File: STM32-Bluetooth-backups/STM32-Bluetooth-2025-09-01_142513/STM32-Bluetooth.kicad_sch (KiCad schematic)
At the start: 41 parts, among them J1 USB_C_Receptacle_USB2.0_16P, J2 TC2030, J3 Conn_01x04, J4 Conn_Coaxial, SW1 SW_Push, U2 STM32WB55CEU6, U3 MIC5365-3.3YD5, X1 32MHz, X2 32kHz768

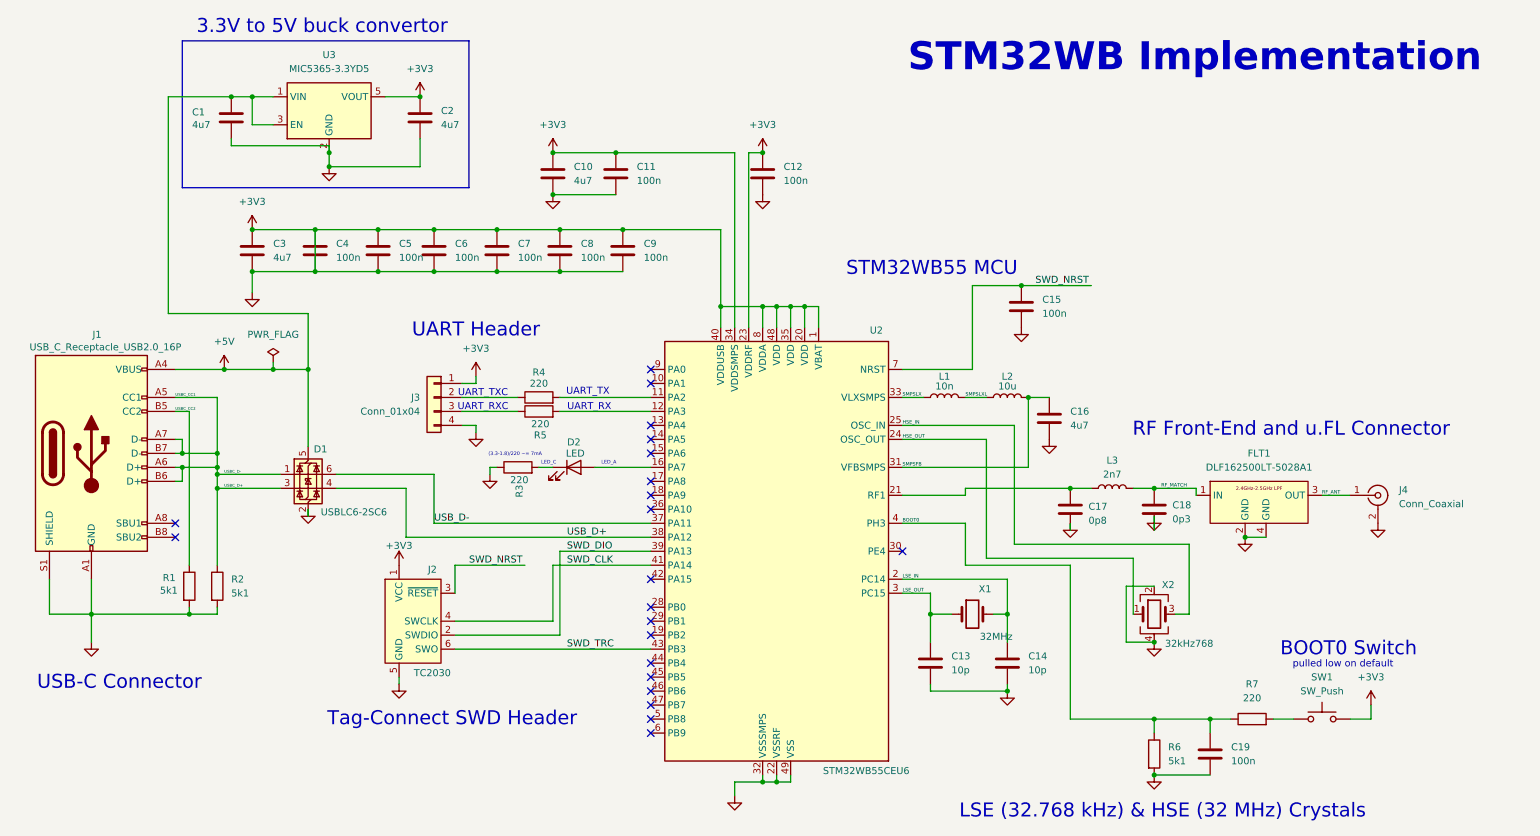
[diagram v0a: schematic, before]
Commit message: Adding net classes and editing footprint library
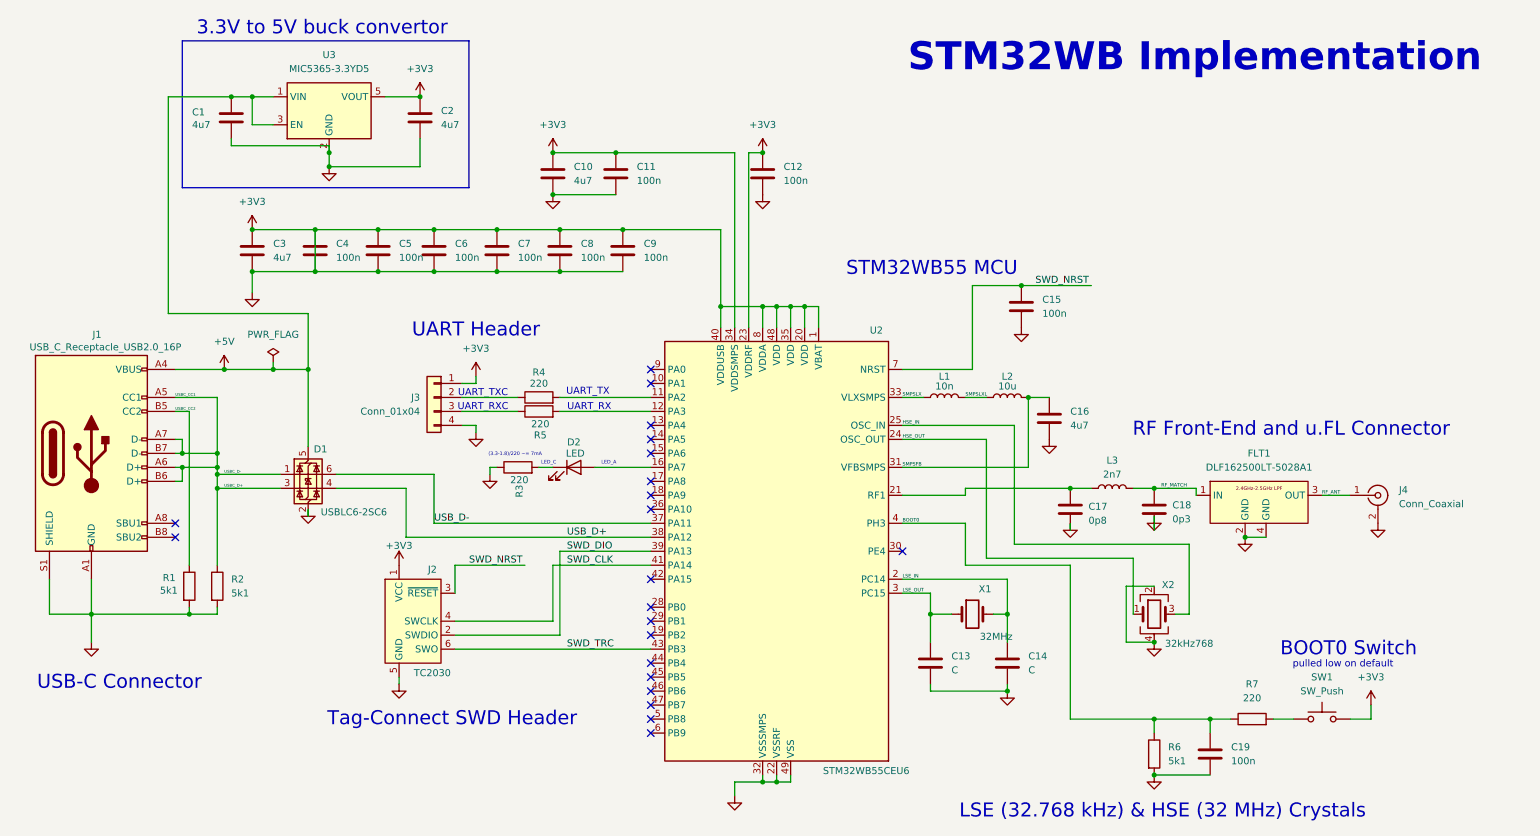
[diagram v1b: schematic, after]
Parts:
- C1, C10, C16, C2, C3: footprint Capacitor_SMD:C_0603_1608Metric -> (none)
- C11, C12, C15, C17, C18, C19, C4, C5, C6, C7, C8, C9: footprint Capacitor_SMD:C_0402_1005Metric -> (none)
- C13, C14: value 10p -> C; footprint Capacitor_SMD:C_0402_1005Metric -> (none)
- D2: footprint LED_SMD:LED_0402_1005Metric -> (none)
- J1: footprint Connector_USB:USB_C_Receptacle_GCT_USB4105-xx-A_16P_TopMnt_Horizontal -> (none)
- J3: footprint Connector_Molex:Molex_PicoBlade_53048-0410_1x04_P1.25mm_Horizontal -> (none)
- J4: footprint Connector_Coaxial:U.FL_Hirose_U.FL-R-SMT-1_Vertical -> (none)
- L1, L3: footprint Inductor_SMD:L_0402_1005Metric -> (none)
- L2: footprint Inductor_SMD:L_0805_2012Metric -> (none)
- R1, R2, R3, R4, R5, R6, R7: footprint Resistor_SMD:R_0402_1005Metric -> (none)
- SW1: footprint Button_Switch_SMD:SW_SPST_CK_RS282G05A3 -> (none)
- X1: footprint Crystal:Crystal_SMD_2016-4Pin_2.0x1.6mm -> (none)
- X2: footprint Crystal:Crystal_SMD_2012-2Pin_2.0x1.2mm -> (none)
